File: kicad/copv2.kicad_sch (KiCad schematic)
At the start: 32 parts, among them J1 Conn_02x03_Counter_Clockwise, Q1 DMP3098LSD-13, U1 ATtiny84A-SS, U2 LM393, U3 LM78M05_TO252

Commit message: add cap on 2.5V
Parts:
- added C6: 100n, Capacitor_SMD:C_0603_1608Metric, symbol Device:C
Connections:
- net +2V5: now also C6.1
- net GND: now also C6.2
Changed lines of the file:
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@@
+	)
+	(junction
+		(at 196.85 73.66)
+		(diameter 0)
+		(color 0 0 0 0)
 	)
 	(junction
@@
 	(wire
 		(pts
+			(xy 196.85 73.66) (xy 205.74 73.66)
+		)
+		(stroke
+			(width 0)
+			(type default)
+		)
+	)
+	(wire
+		(pts
 			(xy 68.58 59.69) (xy 68.58 69.85)
 		)
@@
 		(pts
 			(xy 191.77 66.04) (xy 196.85 66.04)
+		)
+		(stroke
+			(width 0)
+			(type default)
+		)
+	)
+	(wire
+		(pts
+			(xy 196.85 66.04) (xy 205.74 66.04)
 		)
 		(stroke
@@
 					(unit 1)
 				)
+			)
+		)
+	)
+	(symbol
+		(lib_id "Device:C")
+		(at 205.74 69.85 0)
+		(unit 1)
+		(exclude_from_sim no)
+		(in_bom yes)
+		(on_board yes)
+		(dnp no)
+		(fields_autoplaced yes)
+		(property "Reference" "C6"
+			(at 209.55 68.5799 0)
+			(effects
+				(font
+					(size 1.27 1.27)
+				)
+				(justify left)
+			)
+		)
+		(property "Value" "100n"
+			(at 209.55 71.1199 0)
+			(effects
+				(font
+					(size 1.27 1.27)
+				)
+				(justify left)
+			)
+		)
+		(property "Footprint" "Capacitor_SMD:C_0603_1608Metric"
+			(at 206.7052 73.66 0)
+			(effects
+				(font
+					(size 1.27 1.27)
+				)
+				(hide yes)
+			)
+		)
+		(property "Datasheet" "~"
+			(at 205.74 69.85 0)
+			(effects
+				(font
+					(size 1.27 1.27)
+				)
+				(hide yes)
+			)
+		)
+		(property "Description" "Unpolarized capacitor"
+			(at 205.74 69.85 0)
+			(effects
+				(font
+					(size 1.27 1.27)
+				)
+				(hide yes)
+			)
+		)
+		(property "LCSC Part #" "C77055"
+			(at 205.74 69.85 0)
+			(effects
+				(font
+					(size 1.27 1.27)
+				)
+				(hide yes)
+			)
+		)
+		(pin "2"
+		)
+		(pin "1"
+		)
+		(instances
+			(project "copv2"
+				(path "/726ce0f7-60ce-4b01-bd07-dbcd478a7c25"
+					(reference "C6")
+					(unit 1)
+				)

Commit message: fix stuff idk
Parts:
- U2: LCSC Part # (none) -> C32901
- U3: LCSC Part # (none) -> C58069
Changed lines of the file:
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@@
+			)
+		)
+		(property "LCSC Part #" "C32901"
+			(at 120.65 57.15 0)
+			(effects
+				(font
+					(size 1.27 1.27)
+				)
+				(hide yes)
 			)
 		)
@@
 			)
 		)
+		(property "LCSC Part #" "C32901"
+			(at 76.2 72.39 0)
+			(effects
+				(font
+					(size 1.27 1.27)
+				)
+				(hide yes)
+			)
+		)
 		(pin "6"
 		)
@@
 			)
 		)
+		(property "LCSC Part #" "C32901"
+			(at 76.2 44.45 0)
+			(effects
+				(font
+					(size 1.27 1.27)
+				)
+				(hide yes)
+			)
+		)
 		(pin "6"
 		)
@@
 			(at 165.1 66.04 0)
 			(effects
+				(font
+					(size 1.27 1.27)
+				)
+				(hide yes)
+			)
+		)
+		(property "LCSC Part #" "C58069"
+			(at 165.1 66.04 0)
+			(effects

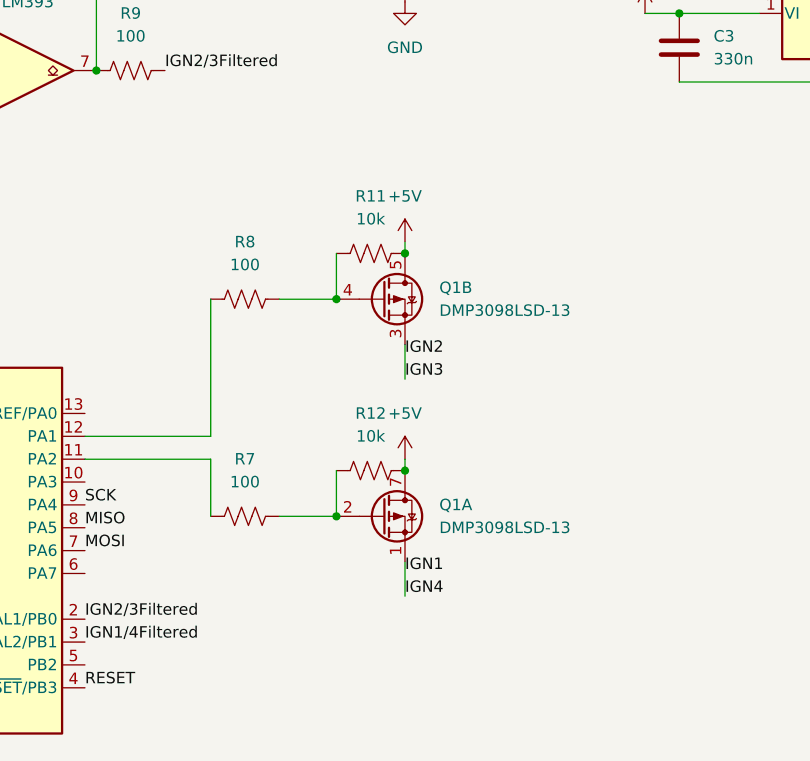
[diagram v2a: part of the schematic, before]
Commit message: mosfet wrong way around
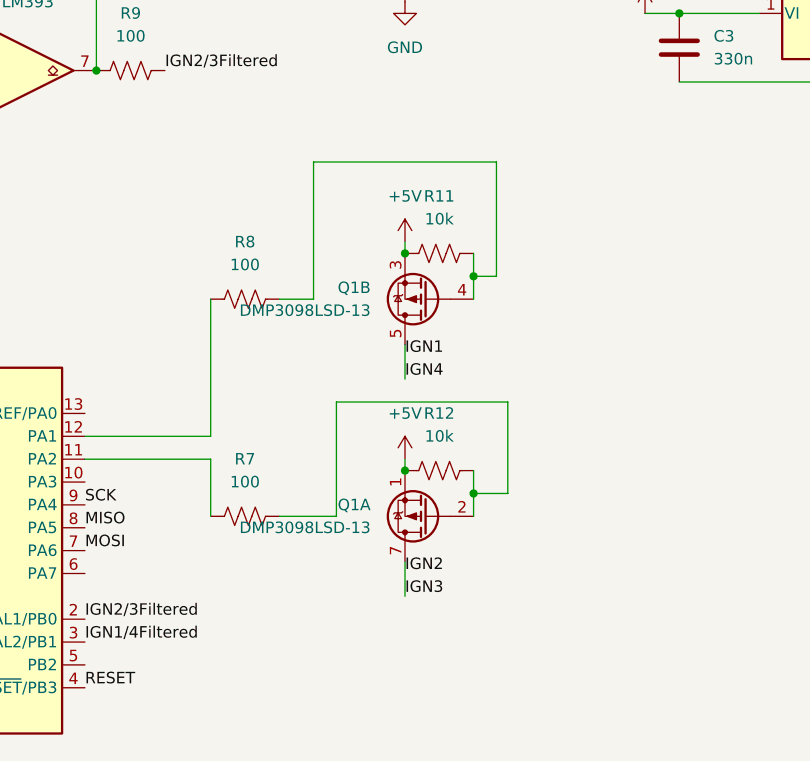
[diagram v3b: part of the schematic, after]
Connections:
- net +5V: now also Q1.1 (S1), Q1.3 (S2); no longer Q1.5 (D2), Q1.6 (D2), Q1.7 (D1), Q1.8 (D1)
- net IGN1: now also Q1.5 (D2), Q1.6 (D2); no longer Q1.1 (S1)
- net IGN2: now also Q1.7 (D1), Q1.8 (D1); no longer Q1.3 (S2)
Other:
- moved on the sheet: Q1A, Q1B, R11, R12
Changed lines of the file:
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@@
 	(paper "A4")
 	(junction
+		(at 118.11 116.84)
+		(diameter 0)
+		(color 0 0 0 0)
+	)
+	(junction
 		(at 177.8 73.66)
 		(diameter 0)
@@
 	)
 	(junction
-		(at 165.1 73.66)
+		(at 125.73 119.38)
 		(diameter 0)
 		(color 0 0 0 0)
 	)
 	(junction
-		(at 118.11 116.84)
+		(at 165.1 73.66)
 		(diameter 0)
 		(color 0 0 0 0)
 	)
 	(junction
-		(at 110.49 121.92)
+		(at 125.73 95.25)
 		(diameter 0)
 		(color 0 0 0 0)
@@
 	)
 	(junction
-		(at 110.49 97.79)
-		(diameter 0)
-		(color 0 0 0 0)
-	)
-	(junction
 		(at 68.58 41.91)
 		(diameter 0)
@@
 	)
 	(junction
-		(at 118.11 92.71)
+		(at 83.82 72.39)
 		(diameter 0)
 		(color 0 0 0 0)
 	)
 	(junction
-		(at 83.82 72.39)
+		(at 118.11 92.71)
 		(diameter 0)
 		(color 0 0 0 0)
@@
 	(wire
 		(pts
+			(xy 125.73 95.25) (xy 125.73 97.79)
+		)
+		(stroke
+			(width 0)
+			(type default)
+		)
+	)
+	(wire
+		(pts
+			(xy 107.95 97.79) (xy 107.95 82.55)
+		)
+		(stroke
+			(width 0)
+			(type default)
+		)
+	)
+	(wire
+		(pts
 			(xy 43.18 95.25) (xy 54.61 95.25)
 		)
@@
 	(wire
 		(pts
+			(xy 125.73 92.71) (xy 125.73 95.25)
+		)
+		(stroke
+			(width 0)
+			(type default)
+		)
+	)
+	(wire
+		(pts
 			(xy 54.61 69.85) (xy 57.15 69.85)
 		)
@@
 	(wire
 		(pts
+			(xy 118.11 102.87) (xy 118.11 106.68)
+		)
+		(stroke
+			(width 0)
+			(type default)
+		)
+	)
+	(wire
+		(pts
 			(xy 83.82 44.45) (xy 83.82 31.75)
 		)
@@
 	(wire
 		(pts
-			(xy 110.49 92.71) (xy 110.49 97.79)
+			(xy 110.49 121.92) (xy 110.49 109.22)
+		)
+		(stroke
+			(width 0)
+			(type default)
+		)
+	)
+	(wire
+		(pts
+			(xy 118.11 91.44) (xy 118.11 92.71)
 		)
 		(stroke
@@
 	(wire
 		(pts
+			(xy 125.73 119.38) (xy 129.54 119.38)
+		)
+		(stroke
+			(width 0)
+			(type default)
+		)
+	)
+	(wire
+		(pts
 			(xy 236.22 21.59) (xy 236.22 22.86)
 		)
@@
 	(wire
 		(pts
+			(xy 107.95 82.55) (xy 128.27 82.55)
+		)
+		(stroke
+			(width 0)
+			(type default)
+		)
+	)
+	(wire
+		(pts
+			(xy 128.27 95.25) (xy 125.73 95.25)
+		)
+		(stroke
+			(width 0)
+			(type default)
+		)
+	)
+	(wire
+		(pts
 			(xy 54.61 95.25) (xy 67.31 95.25)
 		)
@@
 	(wire
 		(pts
+			(xy 125.73 116.84) (xy 125.73 119.38)
+		)
+		(stroke
+			(width 0)
+			(type default)
+		)
+	)
+	(wire
+		(pts
 			(xy 96.52 115.57) (xy 96.52 121.92)
 		)
@@
 	(wire
 		(pts
-			(xy 118.11 127) (xy 118.11 130.81)
+			(xy 125.73 119.38) (xy 125.73 121.92)
 		)
 		(stroke
@@
 	(wire
 		(pts
-			(xy 118.11 102.87) (xy 118.11 106.68)
+			(xy 129.54 109.22) (xy 129.54 119.38)
 		)
 		(stroke
@@
 	(wire
 		(pts
-			(xy 104.14 97.79) (xy 110.49 97.79)
+			(xy 110.49 109.22) (xy 129.54 109.22)
+		)
+		(stroke
+			(width 0)
+			(type default)
+		)
+	)
+	(wire
+		(pts
+			(xy 107.95 97.79) (xy 104.14 97.79)
 		)
 		(stroke
@@
 	(wire
 		(pts
-			(xy 110.49 116.84) (xy 110.49 121.92)
+			(xy 118.11 127) (xy 118.11 130.81)
 		)
 		(stroke
@@
 	(wire
 		(pts
-			(xy 118.11 91.44) (xy 118.11 92.71)
+			(xy 218.44 21.59) (xy 218.44 22.86)
 		)
 		(stroke
@@
 	(wire
 		(pts
-			(xy 218.44 21.59) (xy 218.44 22.86)
+			(xy 118.11 115.57) (xy 118.11 116.84)
 		)
 		(stroke
@@
 	(wire
 		(pts
-			(xy 118.11 115.57) (xy 118.11 116.84)
+			(xy 82.55 115.57) (xy 96.52 115.57)
 		)
 		(stroke
@@
 	(wire
 		(pts
-			(xy 82.55 115.57) (xy 96.52 115.57)
+			(xy 104.14 121.92) (xy 110.49 121.92)
 		)
 		(stroke
@@
 	(wire
 		(pts
-			(xy 104.14 121.92) (xy 110.49 121.92)
+			(xy 156.21 27.94) (xy 167.64 27.94)
 		)
 		(stroke
@@
 	(wire
 		(pts
-			(xy 156.21 27.94) (xy 167.64 27.94)
+			(xy 128.27 82.55) (xy 128.27 95.25)
 		)
 		(stroke
@@
 	)
 	(label "IGN4"
-		(at 118.11 130.81 0)
+		(at 118.11 106.68 0)
 		(effects
 			(font
@@
 	)
 	(label "IGN3"
-		(at 118.11 106.68 0)
+		(at 118.11 130.81 0)
 		(effects
 			(font
@@
 	)
 	(label "IGN1"
-		(at 118.11 128.27 0)
+		(at 118.11 104.14 0)
 		(effects
 			(font
@@
 	)
 	(label "IGN2"
-		(at 118.11 104.14 0)
+		(at 118.11 128.27 0)
 		(effects
 			(font
@@
 	(symbol
 		(lib_id "Device:R_US")
-		(at 114.3 116.84 90)
+		(at 121.92 116.84 270)
 		(unit 1)
 		(exclude_from_sim no)
@@
 		(fields_autoplaced yes)
 		(property "Reference" "R12"
-			(at 114.3 110.49 90)
+			(at 121.92 110.49 90)
 			(effects
 				(font
@@
 		)
 		(property "Value" "10k"
-			(at 114.3 113.03 90)
+			(at 121.92 113.03 90)
 			(effects
 				(font
@@
 		)
 		(property "Footprint" "Resistor_SMD:R_0603_1608Metric"
-			(at 114.554 115.824 90)
+			(at 121.666 117.856 90)
 			(effects
 				(font
@@
 		)
 		(property "Datasheet" "~"
-			(at 114.3 116.84 0)
+			(at 121.92 116.84 0)
 			(effects
 				(font
@@
 		)
 		(property "Description" "Resistor, US symbol"
-			(at 114.3 116.84 0)
+			(at 121.92 116.84 0)
 			(effects
 				(font
@@
 		)
 		(property "LCSC Part #" "C98220"
-			(at 114.3 116.84 90)
+			(at 121.92 116.84 90)
 			(effects
 				(font
@@
 	(symbol
 		(lib_id "Transistor_FET:DMP6050SSD")
-		(at 115.57 121.92 0)
+		(at 120.65 121.92 180)
 		(unit 1)
 		(exclude_from_sim no)
@@
 		(fields_autoplaced yes)
 		(property "Reference" "Q1"
-			(at 121.92 120.6499 0)
+			(at 114.3 120.6499 0)
 			(effects
 				(font
@@
 		)
 		(property "Value" "DMP3098LSD-13"
-			(at 121.92 123.1899 0)
+			(at 114.3 123.1899 0)
 			(effects
 				(font
@@
 		)
 		(property "Footprint" "Package_SO:SOIC-8_3.9x4.9mm_P1.27mm"
-			(at 120.65 123.825 0)
+			(at 115.57 120.015 0)
 			(effects
 				(font
@@
 		)
 		(property "Datasheet" "https://www.diodes.com/assets/Datasheets/DMP6050SSD.pdf"
-			(at 120.65 125.73 0)
+			(at 115.57 118.11 0)
 			(effects
 				(font
@@
 		)
 		(property "Description" "-11.3A Id, -60V Vds, P-Channel Power MOSFET, 55mOhm Ron, 11.9nC Qg (typ), SO-8"
-			(at 115.57 121.92 0)
+			(at 120.65 121.92 0)
 			(effects
 				(font
@@
 		)
 		(property "LCSC Part #" "C531177"
-			(at 115.57 121.92 0)
+			(at 120.65 121.92 0)
 			(effects
 				(font
@@
 	(symbol
 		(lib_id "Transistor_FET:DMP6050SSD")
-		(at 115.57 97.79 0)
+		(at 120.65 97.79 180)
 		(unit 2)
 		(exclude_from_sim no)
@@
 		(fields_autoplaced yes)
 		(property "Reference" "Q1"
-			(at 121.92 96.5199 0)
+			(at 114.3 96.5199 0)
 			(effects
 				(font
@@
 		)
 		(property "Value" "DMP3098LSD-13"
-			(at 121.92 99.0599 0)
+			(at 114.3 99.0599 0)
 			(effects
 				(font
@@
 		)
 		(property "Footprint" "Package_SO:SOIC-8_3.9x4.9mm_P1.27mm"
-			(at 120.65 99.695 0)
+			(at 115.57 95.885 0)
 			(effects
 				(font
@@
 		)
 		(property "Datasheet" "https://www.diodes.com/assets/Datasheets/DMP6050SSD.pdf"
-			(at 120.65 101.6 0)
+			(at 115.57 93.98 0)
 			(effects
 				(font
@@
 		)
 		(property "Description" "-11.3A Id, -60V Vds, P-Channel Power MOSFET, 55mOhm Ron, 11.9nC Qg (typ), SO-8"
-			(at 115.57 97.79 0)
+			(at 120.65 97.79 0)
 			(effects
 				(font
@@
 		)
 		(property "LCSC Part #" "C531177"
-			(at 115.57 97.79 0)
+			(at 120.65 97.79 0)
 			(effects
 				(font
@@
 	(symbol
 		(lib_id "Device:R_US")
-		(at 114.3 92.71 90)
+		(at 121.92 92.71 270)
 		(unit 1)
 		(exclude_from_sim no)
@@
 		(fields_autoplaced yes)
 		(property "Reference" "R11"
-			(at 114.3 86.36 90)
+			(at 121.92 86.36 90)
 			(effects
 				(font
@@
 		)
 		(property "Value" "10k"
-			(at 114.3 88.9 90)
+			(at 121.92 88.9 90)
 			(effects
 				(font
@@
 		)
 		(property "Footprint" "Resistor_SMD:R_0603_1608Metric"
-			(at 114.554 91.694 90)
+			(at 121.666 93.726 90)
 			(effects
 				(font
@@
 		)
 		(property "Datasheet" "~"
-			(at 114.3 92.71 0)
+			(at 121.92 92.71 0)
 			(effects
 				(font
@@
 		)
 		(property "Description" "Resistor, US symbol"
-			(at 114.3 92.71 0)
+			(at 121.92 92.71 0)
 			(effects
 				(font
@@
 		)
 		(property "LCSC Part #" "C98220"
-			(at 114.3 92.71 90)
+			(at 121.92 92.71 90)
 			(effects
 				(font
